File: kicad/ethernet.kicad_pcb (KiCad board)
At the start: 2 copper layers, 120 x 90 mm, 50 parts, among them J1 RJ45_Abracon_ARJP11A-MASA-B-A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, J2 Conn_Coaxial, J3 JTAG, SW1 KSC701, SW2 KSC701, U1 MSP432E401Y, U2 MAX-8Q, Y1 NX3225GA-25.000M-STD-CRG-2

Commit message: updating schematic
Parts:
- removed BT4: NiMH, Battery:BatteryHolder_Keystone_2466_1xAAA
- removed R15: 110k, Resistor_SMD:R_0805_2012Metric
- removed R19: 330k, Resistor_SMD:R_0805_2012Metric
- moved BT2 132.0 mm to (54.2, 73.0)
- moved TR1 113.5 mm to (218.0, 27.5)
- moved C16 98.8 mm to (237.2, 87.8)
- moved C12 98.0 mm to (201.2, 77.2)
- moved C11 95.4 mm to (206.9, 65.5)
- moved C8 91.5 mm to (225.2, 73.8)
- moved BT1 90.0 mm to (99.0, 58.5), turned to 180 degrees
- moved BT3 88.1 mm to (98.8, 88.0), turned to 180 degrees
- moved C13 86.3 mm to (165.5, 126.0)
- moved R8 86.3 mm to (168.0, 126.0)
- moved C6 82.1 mm to (192.8, 67.0)
- moved R13 81.0 mm to (144.0, 138.0), turned to 0 degrees
- moved C17 80.4 mm to (218.5, 93.2)
- moved R14 77.6 mm to (144.0, 135.5), turned to 0 degrees
- moved C9 74.2 mm to (212.5, 84.5)
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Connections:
- U1 pad 15: Net-(U1-Pad15) -> unconnected-(U1-Pad15)
- U1 pad 33: unconnected-(U1-Pad33) -> gTX
- U1 pad 34: unconnected-(U1-Pad34) -> gRX
- U1 pad 40: unconnected-(U1-Pad40) -> gPPS
- U1 pad 41: unconnected-(U1-Pad41) -> ePPS
- U1 pad 71: gPPS -> unconnected-(U1-Pad71)
- U1 pad 72: ePPS -> unconnected-(U1-Pad72)
- U1 pad 95: gTX -> unconnected-(U1-Pad95)
- U1 pad 96: gRX -> unconnected-(U1-Pad96)
- Y1 pad 2: unconnected-(Y1-Pad2) -> GND
- Y1 pad 4: (no net) -> GND
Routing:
- net ~{WAKE}: track 43.8 -> 0.00 mm, vias 2 -> 0
- net gPPS: track 7.72 -> 30.6 mm
- net ~{RST}: track 66.7 -> 45.0 mm, vias 2 -> 0
- net Net-(U1-Pad74): track 18.4 -> 0.00 mm, vias 2 -> 0
- net Net-(J2-Pad1): track 29.9 -> 12.5 mm
- net Net-(J1-Pad3): track 19.5 -> 34.3 mm
- net Net-(U1-Pad73): track 12.7 -> 0.00 mm, vias 2 -> 0
- net Net-(J1-Pad6): track 26.2 -> 38.9 mm
- net gRX: track 37.7 -> 25.5 mm
- net gTX: track 36.3 -> 24.3 mm
- net Net-(J3-Pad6): track 19.8 -> 7.99 mm
- net Net-(J3-Pad2): track 19.0 -> 9.04 mm, vias 0 -> 1
- net ETH_LED0: track 36.7 -> 29.2 mm, vias 2 -> 0
- net Net-(J3-Pad4): track 15.4 -> 8.69 mm, vias 0 -> 1
- net Net-(C1-Pad1): track 0.00 -> 6.39 mm
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- added copper zone on F.Cu, net GND

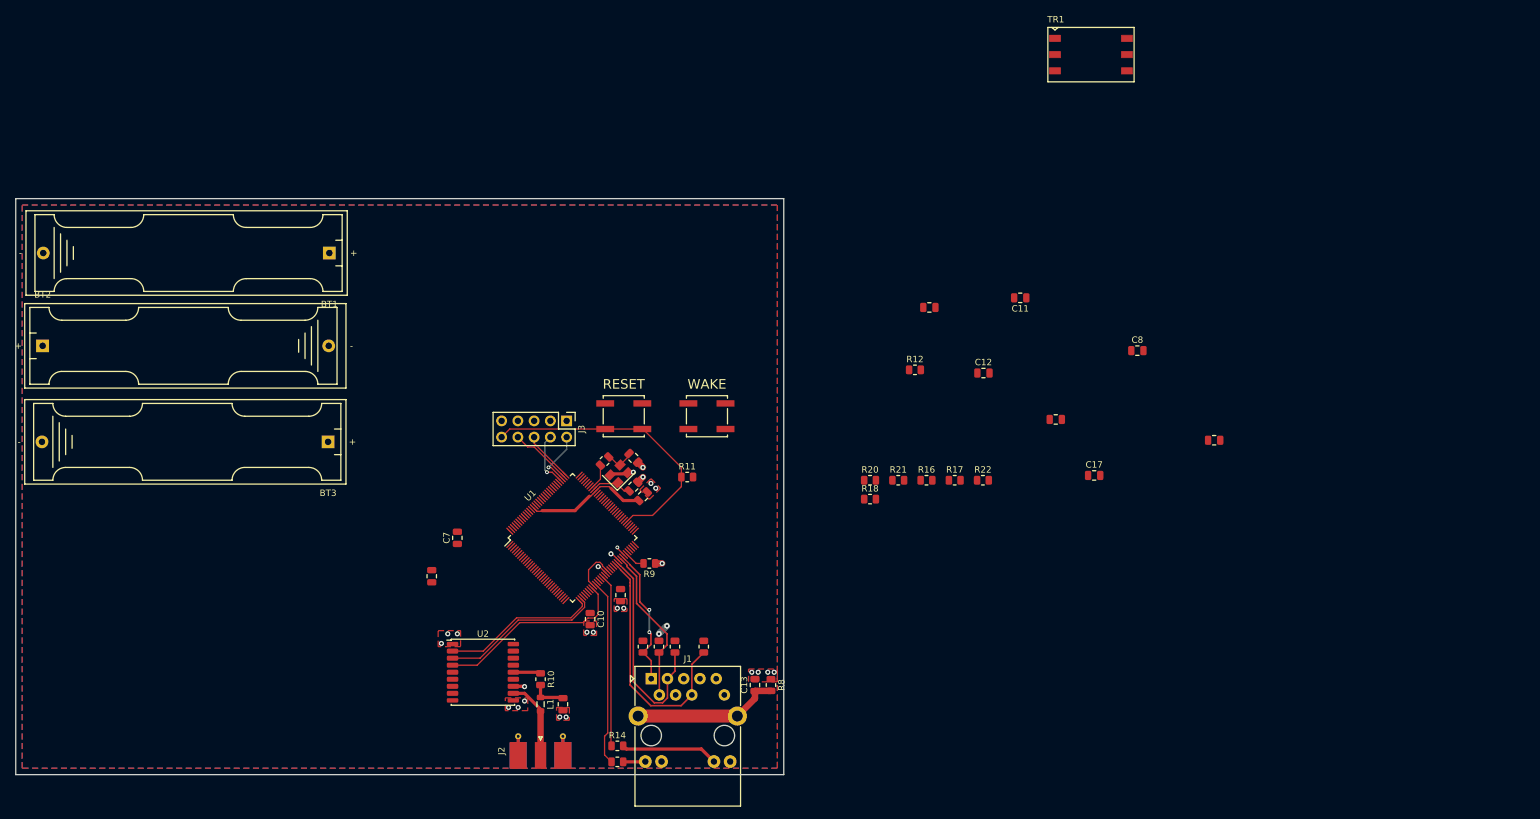
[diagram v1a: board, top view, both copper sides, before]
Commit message: update schematic
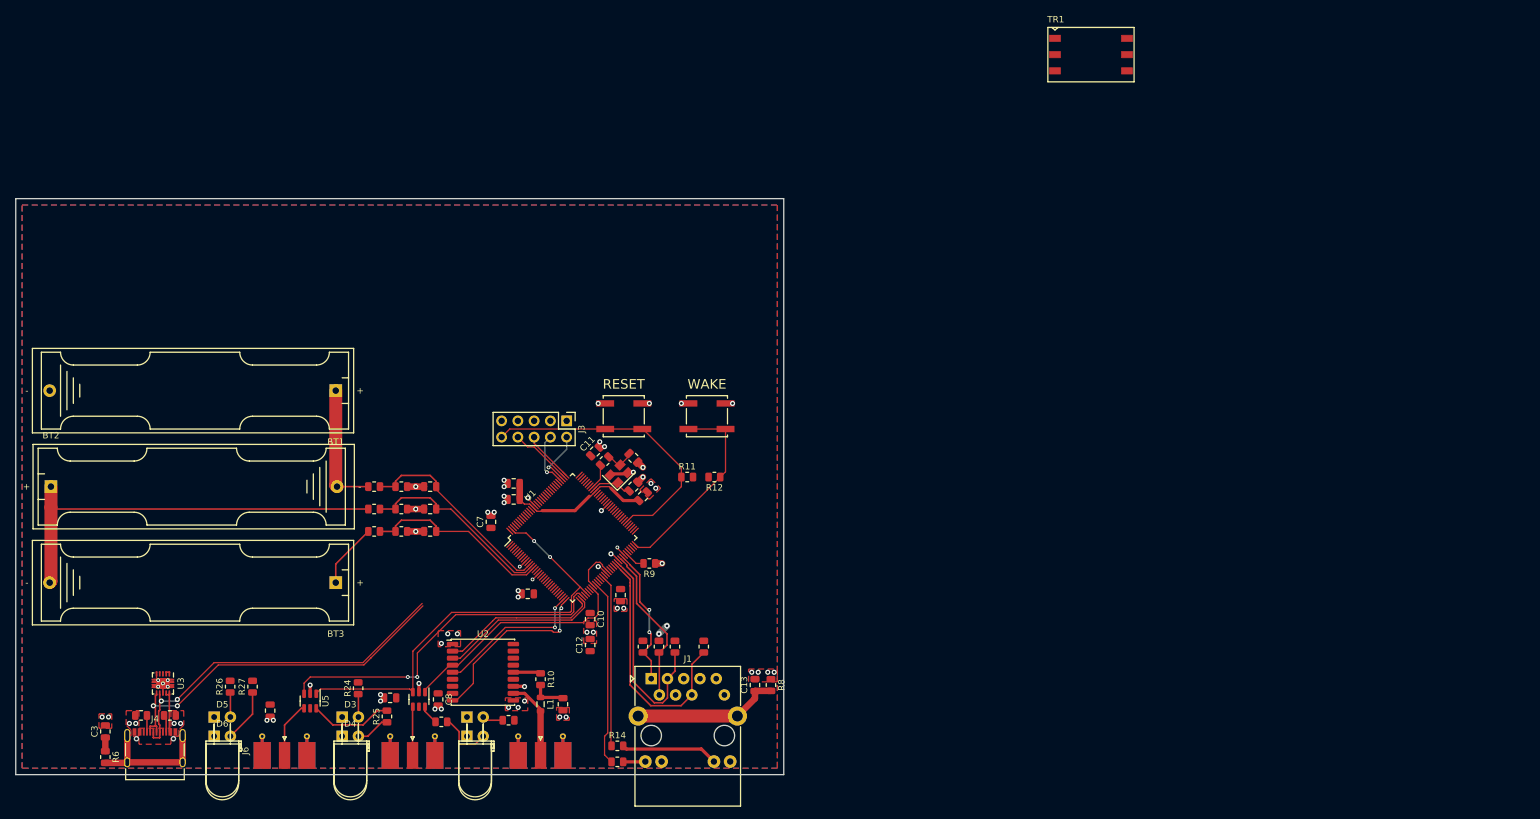
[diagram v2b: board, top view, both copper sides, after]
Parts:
- added C18: 10n, Capacitor_SMD:C_0805_2012Metric, F.Cu at (114.8, 102.0)
- added C19: 10n, Capacitor_SMD:C_0805_2012Metric, F.Cu at (114.8, 98.5)
- added C20: 10n, Capacitor_SMD:C_0805_2012Metric, F.Cu at (114.8, 95.0)
- added C3: 100n, Capacitor_SMD:C_0805_2012Metric, F.Cu at (64.0, 133.2)
- added D1: LED, LED_THT:LED_D5.0mm_Horizontal_O3.81mm_Z3.0mm, F.Cu at (120.5, 131.0)
- added D2: LED, LED_THT:LED_D5.0mm_Horizontal_O1.27mm_Z3.0mm, F.Cu at (120.5, 134.0)
- added D3: LED, LED_THT:LED_D5.0mm_Horizontal_O3.81mm_Z3.0mm, F.Cu at (101.0, 131.0)
- added D4: LED, LED_THT:LED_D5.0mm_Horizontal_O1.27mm_Z3.0mm, F.Cu at (101.0, 134.0)
- added D5: LED, LED_THT:LED_D5.0mm_Horizontal_O3.81mm_Z3.0mm, F.Cu at (81.0, 131.0)
- added D6: LED, LED_THT:LED_D5.0mm_Horizontal_O1.27mm_Z3.0mm, F.Cu at (81.0, 134.0)
- added J4: USB_C_Receptacle_USB2.0, Connector_USB:USB_C_Receptacle_XKB_U262-16XN-4BVC11, F.Cu at (71.8, 137.0)
- added J5: Conn_Coaxial, Connector_Coaxial:SMA_Molex_73251-2120_EdgeMount_Horizontal, F.Cu at (112.0, 137.0)
- added J6: Conn_Coaxial, Connector_Coaxial:SMA_Molex_73251-2120_EdgeMount_Horizontal, F.Cu at (92.0, 137.0)
- added R15: 5.1k, Resistor_SMD:R_0805_2012Metric, F.Cu at (74.1, 130.8)
- added R19: 330, Resistor_SMD:R_0805_2012Metric, F.Cu at (127.0, 131.5)
- added R23: 330, Resistor_SMD:R_0805_2012Metric, F.Cu at (116.5, 131.8)
- added R24: 330, Resistor_SMD:R_0805_2012Metric, F.Cu at (103.5, 126.5)
- added R25: 330, Resistor_SMD:R_0805_2012Metric, F.Cu at (108.0, 130.9)
- added R26: 330, Resistor_SMD:R_0805_2012Metric, F.Cu at (83.5, 126.2)
- added R27: 330, Resistor_SMD:R_0805_2012Metric, F.Cu at (87.0, 126.2)
- added R6: 49.9, Resistor_SMD:R_0805_2012Metric, F.Cu at (64.0, 137.2)
- added R7: 5.1k, Resistor_SMD:R_0805_2012Metric, F.Cu at (69.6, 130.8)
- added U3: TPD4S014, Package_SON:Texas_S-PWSON-N10, F.Cu at (73.0, 125.8)
- added U4: 74AUC2G34, Package_TO_SOT_SMD:SOT-23-6, F.Cu at (113.0, 128.2)
- added U5: 74AUC2G34, Package_TO_SOT_SMD:SOT-23-6, F.Cu at (96.0, 128.5)
- R20, R21, R22: value 330k -> 220k
- moved C8 122.1 mm to (116.0, 128.2), turned to -90 degrees
- moved C6 120.7 mm to (89.8, 130.0), turned to -90 degrees
- moved C9 112.7 mm to (108.5, 128.0), turned to 180 degrees
- moved C16 109.8 mm to (127.8, 97.0), turned to 180 degrees
- moved R22 95.1 mm to (106.0, 95.0)
- moved C17 90.7 mm to (127.8, 94.5), turned to 180 degrees
- moved R17 86.6 mm to (110.2, 98.5)
- moved R16 82.4 mm to (110.2, 102.0)
- moved R21 82.0 mm to (106.0, 98.5)
- moved R20 77.9 mm to (106.0, 102.0)
- moved C12 74.7 mm to (139.8, 119.8), turned to 90 degrees
- moved R18 73.3 mm to (110.2, 95.0)
- moved C11 70.7 mm to (140.5, 89.5), turned to 45 degrees
- moved R12 35.5 mm to (159.2, 93.5), turned to 180 degrees
- moved BT2 22.0 mm to (55.5, 95.0)
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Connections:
- net Net-(BT3-Pad1) renamed +BATT
- C10 pad 1: +3V3 -> VCC
- C11 pad 1: +3V3 -> VCC
- C12 pad 1: +3V3 -> VCC
- C4 pad 1: +3V3 -> VCC
- C5 pad 1: +3V3 -> VCC
- C6 pad 1: +3V3 -> VCC
- C7 pad 1: +3V3 -> VCC
- C8 pad 1: +3V3 -> VCC
- C9 pad 1: +3V3 -> VCC
- J1 pad 4: +3V3 -> VCC
- J1 pad 5: +3V3 -> VCC
- J3 pad 1: +3V3 -> VCC
- R1 pad 2: +3V3 -> VCC
- R11 pad 2: +3V3 -> VCC
- R12 pad 2: +3V3 -> VCC
- R2 pad 1: +3V3 -> VCC
- R3 pad 2: +3V3 -> VCC
- R4 pad 1: +3V3 -> VCC
- U1 pad 101: +3V3 -> VCC
- U1 pad 102: +3V3 -> VCC
- U1 pad 103: +3V3 -> VCC
- U1 pad 104: +3V3 -> VCC
- U1 pad 105: +3V3 -> VCC
- U1 pad 106: +3V3 -> VCC
- U1 pad 107: +3V3 -> VCC
- U1 pad 108: +3V3 -> VCC
- U1 pad 109: +3V3 -> VCC
- U1 pad 110: +3V3 -> VCC
- U1 pad 111: +3V3 -> VCC
- U1 pad 112: +3V3 -> VCC
- U1 pad 113: +3V3 -> VCC
- U1 pad 122: +3V3 -> VCC
- U1 pad 127: unconnected-(U1-Pad127) -> uPPS
- U1 pad 16: +3V3 -> VCC
- U1 pad 26: +3V3 -> VCC
- U1 pad 28: +3V3 -> VCC
- U1 pad 31: unconnected-(U1-Pad31) -> Net-(U2-Pad5)
- U1 pad 32: unconnected-(U1-Pad32) -> Net-(U2-Pad9)
- U1 pad 35: unconnected-(U1-Pad35) -> uFRQ
- U1 pad 36: unconnected-(U1-Pad36) -> VCC
- U1 pad 37: unconnected-(U1-Pad37) -> uPPS
- U1 pad 38: unconnected-(U1-Pad38) -> VCC
- U1 pad 39: +3V3 -> VCC
- U1 pad 43: +3V3 -> VCC
- U1 pad 44: +3V3 -> VCC
- U1 pad 45: +3V3 -> VCC
- U1 pad 47: +3V3 -> VCC
- U1 pad 50: +3V3 -> VCC
- U1 pad 51: +3V3 -> VCC
- U1 pad 52: +3V3 -> VCC
- U1 pad 60: +3V3 -> VCC
- U1 pad 61: +3V3 -> VCC
- U1 pad 62: +3V3 -> VCC
- U1 pad 63: +3V3 -> VCC
- U1 pad 68: +3V3 -> VCC
- U1 pad 69: +3V3 -> VCC
- U1 pad 7: +3V3 -> VCC
- U1 pad 73: Net-(U1-Pad73) -> unconnected-(U1-Pad73)
- U1 pad 74: Net-(U1-Pad74) -> unconnected-(U1-Pad74)
- U1 pad 75: +3V3 -> VCC
- U1 pad 76: +3V3 -> VCC
- U1 pad 77: +3V3 -> VCC
- U1 pad 78: +3V3 -> VCC
- U1 pad 79: +3V3 -> VCC
- U1 pad 8: +3V3 -> VCC
- U1 pad 81: +3V3 -> VCC
- U1 pad 82: +3V3 -> VCC
- U1 pad 83: +3V3 -> VCC
- U1 pad 84: +3V3 -> VCC
- U1 pad 85: +3V3 -> VCC
- U1 pad 86: +3V3 -> VCC
- U1 pad 9: +3V3 -> VCC
- U1 pad 90: +3V3 -> VCC
- U1 pad 91: +3V3 -> VCC
- U1 pad 92: +3V3 -> VCC
- U1 pad 93: +3V3 -> D-
- U1 pad 94: +3V3 -> D+
- U2 pad 5: Net-(U1-Pad73) -> Net-(U2-Pad5)
- U2 pad 6: +3V3 -> VCC
- U2 pad 7: +3V3 -> VCC
- U2 pad 8: +3V3 -> VCC
- U2 pad 9: Net-(U1-Pad74) -> Net-(U2-Pad9)
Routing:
- net uPPS: track 0.00 -> 69.6 mm, vias 0 -> 2
- net Net-(BT2-Pad1): track 0.00 -> 64.8 mm
- net D-: track 0.00 -> 56.4 mm, vias 0 -> 2
- net D+: track 0.00 -> 55.8 mm, vias 0 -> 2
- net uFRQ: track 0.00 -> 54.8 mm, vias 0 -> 2
- net Net-(R18-Pad1): track 0.00 -> 31.9 mm
- net ~{WAKE}: track 0.00 -> 31.7 mm
- net Net-(R17-Pad1): track 0.00 -> 30.6 mm
- net Net-(R16-Pad1): track 0.00 -> 29.6 mm
- net Net-(U2-Pad9): track 0.00 -> 28.3 mm, vias 0 -> 2
- net GND: track 14.1 -> 39.3 mm, vias 26 -> 66
- net Net-(U2-Pad5): track 0.00 -> 24.0 mm, vias 0 -> 2
- net Net-(J4-PadS1): track 0.00 -> 20.5 mm
- net Net-(BT1-Pad1): track 0.00 -> 20.0 mm
- net Net-(R25-Pad2): track 0.00 -> 13.0 mm
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- added copper zone on F.Cu, net /VBUS
- added copper zone on F.Cu, net VCC
- removed copper zone on F.Cu, net +3V3

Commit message: simulating poe
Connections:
- net VCC renamed +3V3

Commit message: poe supply design
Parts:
- added C21: 10u, Capacitor_SMD:C_0805_2012Metric, F.Cu at (118.8, 57.8)
- added C22: 10u, Capacitor_SMD:C_0805_2012Metric, F.Cu at (73.8, 54.5)
- added C23: 100n, Capacitor_SMD:C_0805_2012Metric, F.Cu at (73.8, 58.0)
- added C24: 100n, Capacitor_SMD:C_0805_2012Metric, F.Cu at (118.8, 54.7)
- added D7: MBR0520L, Diode_SMD:D_SOD-123, F.Cu at (78.8, 59.5)
- added D8: MBR0520L, Diode_SMD:D_SOD-123, F.Cu at (78.8, 54.5)
- added Q1: BSO220N03MD, Package_SO:SOIC-8_3.9x4.9mm_P1.27mm, F.Cu at (112.3, 56.5)
- added R28: 10k, Resistor_SMD:R_0805_2012Metric, F.Cu at (77.0, 121.2)
- added R29: 10k, Resistor_SMD:R_0805_2012Metric, F.Cu at (69.5, 120.7)
- added U6: MAX40200AUK, Package_TO_SOT_SMD:SOT-23-5, F.Cu at (67.0, 55.0)
- moved TR1 132.6 mm to (88.8, 57.0), turned to 180 degrees
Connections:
- net Net-(U3-Pad1) renamed +5V
- TR1 pad 1: unconnected-(TR1-Pad1) -> Net-(TR1-Pad1)
- TR1 pad 2: unconnected-(TR1-Pad2) -> Net-(TR1-Pad2)
- TR1 pad 3: unconnected-(TR1-Pad3) -> Net-(TR1-Pad3)
- TR1 pad 4: unconnected-(TR1-Pad4) -> Net-(TR1-Pad4)
- TR1 pad 5: unconnected-(TR1-Pad5) -> GND
- TR1 pad 6: unconnected-(TR1-Pad6) -> Net-(TR1-Pad6)
- U3 pad 3: unconnected-(U3-Pad3) -> Net-(U3-Pad3)
- U3 pad 4: unconnected-(U3-Pad4) -> VUSB
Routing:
- net Net-(TR1-Pad2): track 0.00 -> 16.6 mm
- net +5VP: track 0.00 -> 12.6 mm
- net (no net): track 0.00 -> 5.59 mm
- net Net-(TR1-Pad3): track 0.00 -> 3.40 mm
- net Net-(TR1-Pad1): track 0.00 -> 3.40 mm
- net Net-(TR1-Pad6): track 0.00 -> 2.75 mm
- net Net-(TR1-Pad4): track 0.00 -> 2.75 mm
- net GND: track 39.3 -> 40.7 mm, vias 66 -> 73
- added copper zone on F.Cu, net +5VP

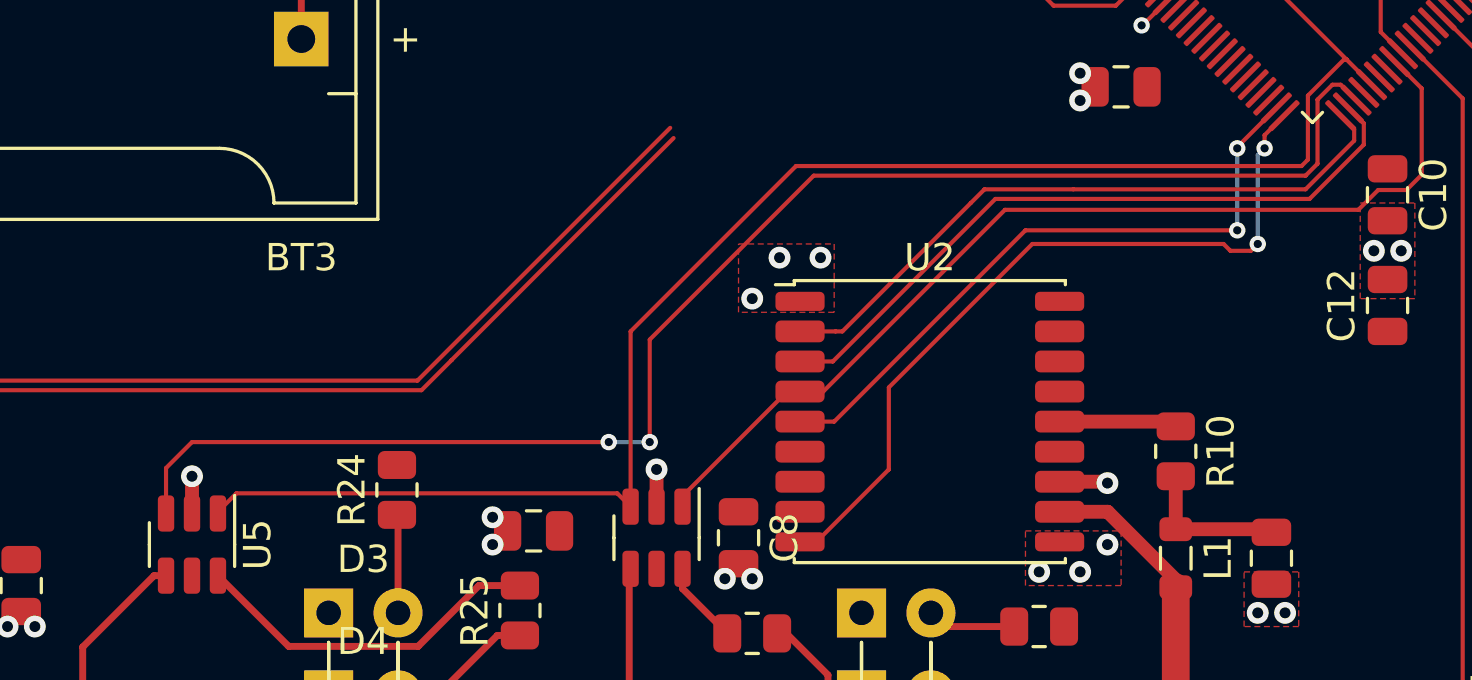
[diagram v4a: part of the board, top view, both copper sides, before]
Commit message: update schematic
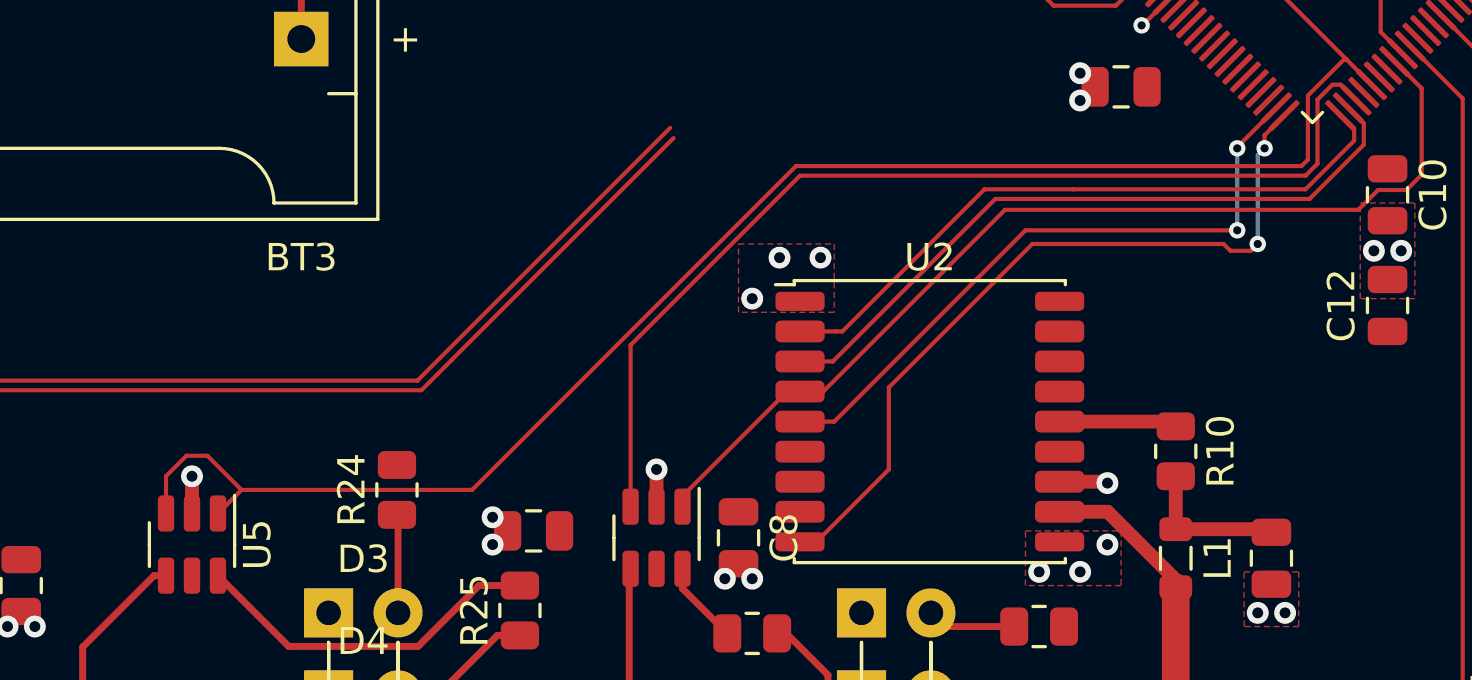
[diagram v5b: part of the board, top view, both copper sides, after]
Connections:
- U4 pad 3: uPPS -> uFRQ
- U5 pad 3: uFRQ -> uPPS
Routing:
- net uFRQ: track 54.8 -> 38.0 mm, vias 2 -> 0
- net uPPS: track 69.6 -> 70.3 mm
